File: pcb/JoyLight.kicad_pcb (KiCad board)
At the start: 2 copper layers, 116.8 x 52.1 mm, 27 parts, among them J1 110990037, J2 110990037, J3 110990037, J4 110990037, J5 Conn_01x07_Male, J6 Conn_01x07_Male, SW1 SW_SPST, SW2 SW_SPST, SW3 SW_SPST, U1 SeeeduinoXIAO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

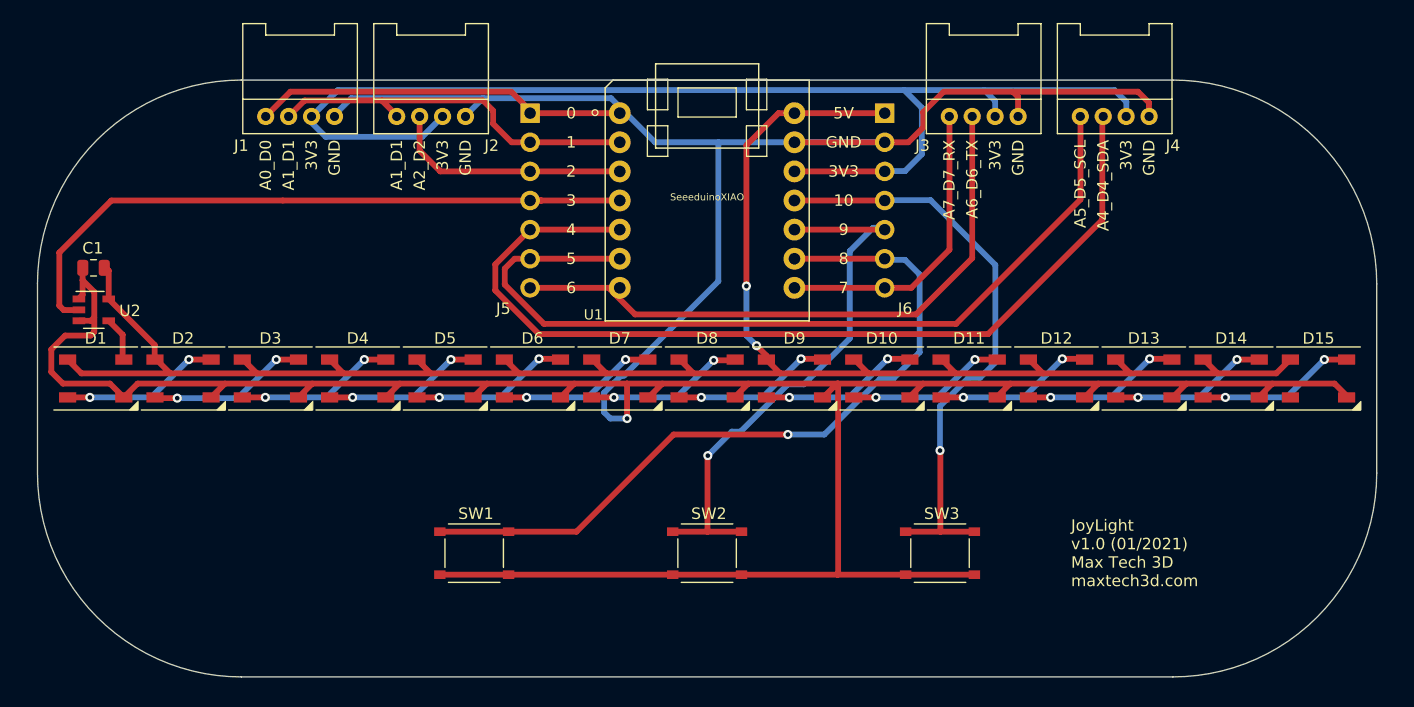
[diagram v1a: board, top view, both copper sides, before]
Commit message: PCB finishing touches
- added mounting points
- added the OSHW logo
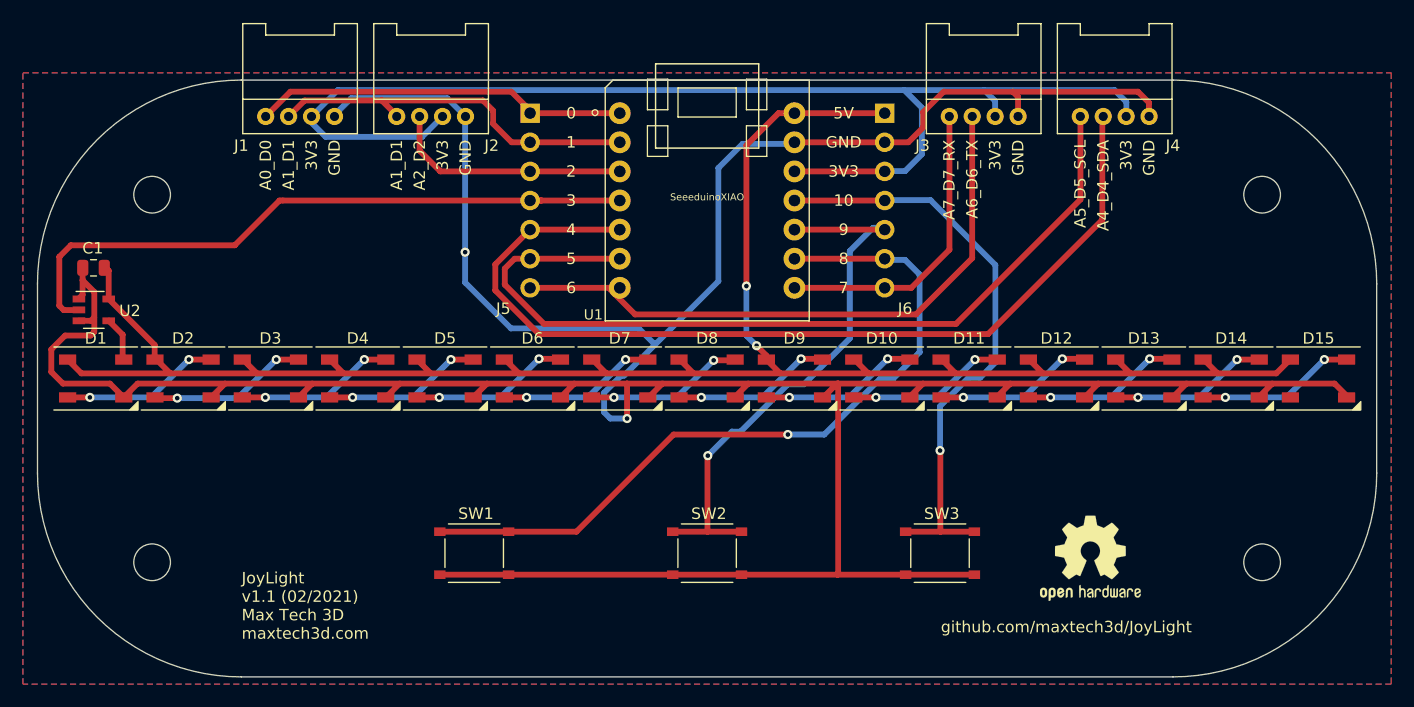
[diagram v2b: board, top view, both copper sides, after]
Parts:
- added H1: MountingHole, MountingHole:MountingHole_3.2mm_M3, F.Cu at (198.3, 138.0)
- added H2: MountingHole, MountingHole:MountingHole_3.2mm_M3, F.Cu at (101.4, 138.0)
- added H3: MountingHole, MountingHole:MountingHole_3.2mm_M3, F.Cu at (198.3, 105.9)
- added H4: MountingHole, MountingHole:MountingHole_3.2mm_M3, F.Cu at (101.4, 105.9)
- added REF**: OSHW-Logo2_9.8x8mm_SilkScreen, Symbol:OSHW-Logo2_9.8x8mm_SilkScreen, B.Cu at (114.3, 137.6)
- added REF**: OSHW-Logo2_9.8x8mm_SilkScreen, Symbol:OSHW-Logo2_9.8x8mm_SilkScreen, F.Cu at (183.3, 137.6)
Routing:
- net GND: track 338.7 -> 337.4 mm, vias 1 -> 2
- added copper zone on B.Cu, net GND
- added copper zone on F.Cu, net GND
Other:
- board text added: "JoyLight v1.1 (02/2021) Max Tech 3D maxtech3d.com"
- board text added: "github.com/maxtech3d/JoyLight"
- board text removed: "JoyLight v1.0 (01/2021) Max Tech 3D maxtech3d.com"

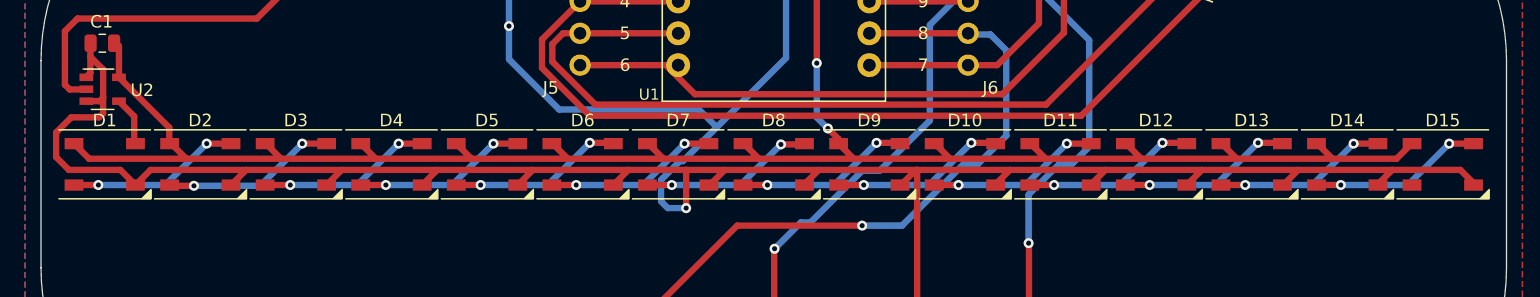
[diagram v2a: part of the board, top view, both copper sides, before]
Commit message: Joylight v1.1 PCB
- minor changes for preparing the board for production
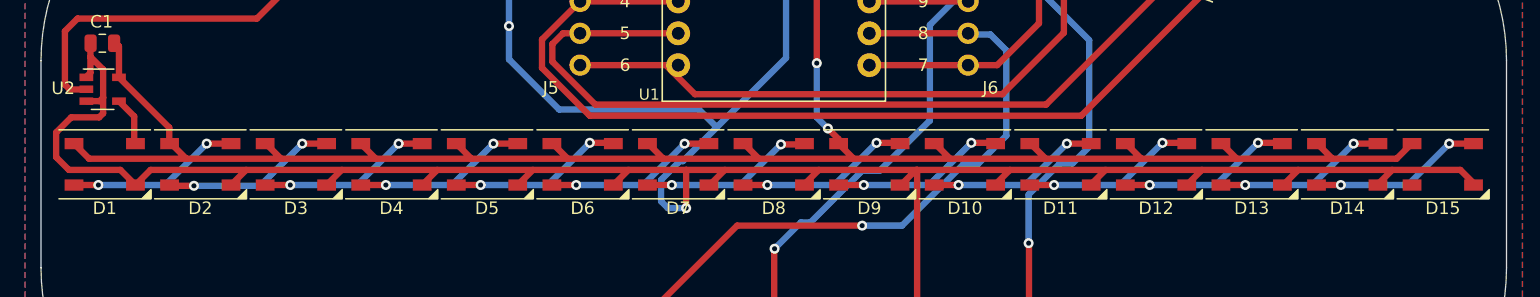
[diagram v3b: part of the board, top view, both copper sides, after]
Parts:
- turned D1 to 180 degrees
- turned D10 to 180 degrees
- turned D11 to 180 degrees
- turned D12 to 180 degrees
- turned D13 to 180 degrees
- turned D14 to 180 degrees
- turned D15 to 180 degrees
- turned D2 to 180 degrees
- turned D3 to 180 degrees
- turned D4 to 180 degrees
- turned D5 to 180 degrees
- turned D6 to 180 degrees
- turned D7 to 180 degrees
- turned D8 to 180 degrees
- turned D9 to 180 degrees
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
